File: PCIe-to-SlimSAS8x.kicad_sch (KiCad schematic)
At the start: 11 parts, among them J1 PCI_Express_x8, J2 OpenCAPI_AAC_Host

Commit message: Initial Layout Complete
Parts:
- renumbered R4 to R3, R3 to R4
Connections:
- net GND: now also J2.MP (Shield)
- net PERn0 renamed Rx0_P
- net PERn1 renamed Rx1_P
- net PERn2 renamed Rx2_P
- net PERn3 renamed Rx3_P
- net PERn4 renamed Rx4_P
- net PERn5 renamed Rx5_P
- net PERn6 renamed Rx6_P
- net PERn7 renamed Rx7_P
- net PERp0 renamed Rx0_N
- net PERp1 renamed Rx1_N
- net PERp2 renamed Rx2_N
- net PERp3 renamed Rx3_N
- net PERp4 renamed Rx4_N
- net PERp5 renamed Rx5_N
- net PERp6 renamed Rx6_N
- net PERp7 renamed Rx7_N
- net PETn0 renamed Tx0_N
- net Tx0_N: now also J2.A2 (Tx0_N); no longer J2.A3 (Tx0_P)
- net PETn1 renamed Tx1_N
- net Tx1_N: now also J2.B2 (Tx1_N); no longer J2.B3 (Tx1_P)
- net PETn2 renamed Tx2_N
- net Tx2_N: now also J2.A5 (Tx2_N); no longer J2.A6 (Tx2_P)
- net PETn3 renamed Tx3_N
- net Tx3_N: now also J2.B5 (Tx3_N); no longer J2.B6 (Tx3_P)
- net PETn4 renamed Tx4_N
- net Tx4_N: now also J2.B11 (Tx4_N); no longer J2.B12 (Tx4_P)
- net PETn5 renamed Tx5_N
- net Tx5_N: now also J2.A14 (Tx5_N); no longer J2.A15 (Tx5_P)
- net PETn6 renamed Tx6_N
- net Tx6_N: now also J2.B14 (Tx6_N); no longer J2.B15 (Tx6_P)
- net PETn7 renamed Tx7_N
- net Tx7_N: now also J2.A17 (Tx7_N); no longer J2.A18 (Tx7_P)
- net PETp0 renamed Tx0_P
- net Tx0_P: now also J2.A3 (Tx0_P); no longer J2.A2 (Tx0_N)
- net PETp1 renamed Tx1_P
- net Tx1_P: now also J2.B3 (Tx1_P); no longer J2.B2 (Tx1_N)
- net PETp2 renamed Tx2_P
- net Tx2_P: now also J2.A6 (Tx2_P); no longer J2.A5 (Tx2_N)
- net PETp3 renamed Tx3_P
- net Tx3_P: now also J2.B6 (Tx3_P); no longer J2.B5 (Tx3_N)
- net PETp4 renamed Tx4_P
- net Tx4_P: now also J2.B12 (Tx4_P); no longer J2.B11 (Tx4_N)
- net PETp5 renamed Tx5_P
- net Tx5_P: now also J2.A15 (Tx5_P); no longer J2.A14 (Tx5_N)
- net PETp6 renamed Tx6_P
- net Tx6_P: now also J2.B15 (Tx6_P); no longer J2.B14 (Tx6_N)
- net PETp7 renamed Tx7_P
- net Tx7_P: now also J2.A18 (Tx7_P); no longer J2.A17 (Tx7_N)
- net REFCLKn renamed REFCLK_N
- net REFCLKp renamed REFCLK_P
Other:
- note added: "SlimSAS 8x Cable flips rows of pins. Row A connects to Row B and vice versa. The OpenCAPI AAC FPGA-based Add-In Card uses the Carrier pinout, which means this adapter should use the Host pinout. FPGA_Card_RX = Host_TX = PCIe_TX FPGA_Card_TX = Host_RX = PCIe_RX"
- note removed: "SlimSAS 8i Cable flips rows of pins. Row A connects to Row B and vice versa. The OpenCAPI AAC Add-In Card uses the Carrier pinout, which means this adapter should use the Host pinout. Card_TX = Host_RX = PCIe_RX Card_RX = Host_TX = PCIe_TX"
- title: PCI-Express to OpenCAPI Adapter -> PCI-Express to SlimSAS 8x Adapter
- moved on the sheet: J1, R1, R2, R3, R4, TP1, TP2, TP3, TP4, TP5

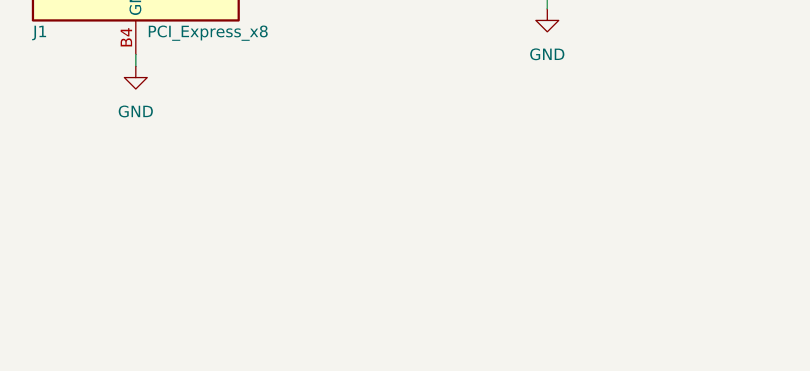
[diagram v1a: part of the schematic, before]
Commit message: Added Microstrip Test Trace
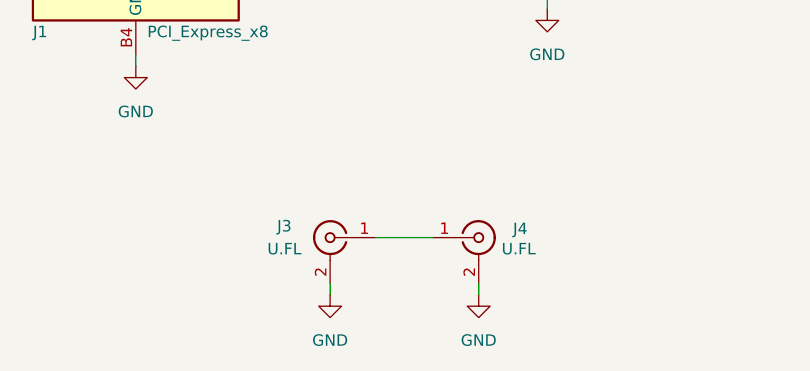
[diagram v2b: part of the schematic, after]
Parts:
- added J3, J4: U.FL, Connector_Coaxial:U.FL_Hirose_U.FL-R-SMT-1_Vertical, symbol Connector:Conn_Coaxial
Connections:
- net GND: now also J3.2 (Ext), J4.2 (Ext)
- new net: J3.1 (In), J4.1 (In)
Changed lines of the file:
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@@
+    (stroke (width 0) (type default) (color 0 0 0 0))
+  )
+  (wire (pts (xy 110.49 175.26) (xy 110.49 176.53))
     (stroke (width 0) (type default) (color 0 0 0 0))
   )
@@
     (stroke (width 0) (type default) (color 0 0 0 0))
   )
+  (wire (pts (xy 127 175.26) (xy 127 176.53))
+    (stroke (width 0) (type default) (color 0 0 0 0))
+  )
   (wire (pts (xy 134.62 142.24) (xy 134.62 144.78))
     (stroke (width 0) (type default) (color 0 0 0 0))
@@
   )
   (wire (pts (xy 171.45 142.24) (xy 176.53 142.24))
+    (stroke (width 0) (type default) (color 0 0 0 0))
+  )
+  (wire (pts (xy 115.57 170.18) (xy 121.92 170.18))
     (stroke (width 0) (type default) (color 0 0 0 0))
   )
@@
     (pin "2")
   )
+  (symbol (lib_id "Connector:Conn_Coaxial") (at 127 170.18 0) (unit 1)
+    (in_bom yes) (on_board yes)
+    (property "Reference" "J4" (id 0) (at 130.81 169.2031 0)
+      (effects (font (size 1.27 1.27)) (justify left))
+    )
+    (property "Value" "U.FL" (id 1) (at 129.54 171.45 0)
+      (effects (font (size 1.27 1.27)) (justify left))
+    )
+    (property "Footprint" "Connector_Coaxial:U.FL_Hirose_U.FL-R-SMT-1_Vertical" (id 2) (at 127 170.18 0)
+      (effects (font (size 1.27 1.27)) hide)
+    )
+    (property "Datasheet" " ~" (id 3) (at 127 170.18 0)
+      (effects (font (size 1.27 1.27)) hide)
+    )
+    (pin "1")
+    (pin "2")
+  )
   (symbol (lib_id "power:GND") (at 88.9 151.13 0) (unit 1)
     (in_bom yes) (on_board yes) (fields_autoplaced)
@@
     (pin "1")
   )
+  (symbol (lib_id "Connector:Conn_Coaxial") (at 110.49 170.18 0) (mirror y) (unit 1)
+    (in_bom yes) (on_board yes)
+    (property "Reference" "J3" (id 0) (at 105.41 168.91 0))
+    (property "Value" "U.FL" (id 1) (at 105.41 171.45 0))
+    (property "Footprint" "Connector_Coaxial:U.FL_Hirose_U.FL-R-SMT-1_Vertical" (id 2) (at 110.49 170.18 0)
+      (effects (font (size 1.27 1.27)) hide)
+    )
+    (property "Datasheet" " ~" (id 3) (at 110.49 170.18 0)
+      (effects (font (size 1.27 1.27)) hide)
+    )
+    (pin "1")
+    (pin "2")
+  )
   (symbol (lib_id "power:GND") (at 134.62 144.78 0) (unit 1)
     (in_bom yes) (on_board yes) (fields_autoplaced)
@@
     (pin "1")
     (pin "2")
+  )
+  (symbol (lib_id "power:GND") (at 127 176.53 0) (unit 1)
+    (in_bom yes) (on_board yes) (fields_autoplaced)
+    (property "Reference" "#PWR0105" (id 0) (at 127 182.88 0)
+      (effects (font (size 1.27 1.27)) hide)
+    )
+    (property "Value" "GND" (id 1) (at 127 181.61 0))
+    (property "Footprint" "" (id 2) (at 127 176.53 0)
+      (effects (font (size 1.27 1.27)) hide)
+    )
+    (property "Datasheet" "" (id 3) (at 127 176.53 0)
+      (effects (font (size 1.27 1.27)) hide)
+    )
+    (pin "1")
   )
   (symbol (lib_id "Connector:Bus_PCI_Express_x8") (at 88.9 104.14 0) (unit 1)
@@
     (pin "B9")
   )
+  (symbol (lib_id "power:GND") (at 110.49 176.53 0) (unit 1)
+    (in_bom yes) (on_board yes) (fields_autoplaced)
+    (property "Reference" "#PWR0106" (id 0) (at 110.49 182.88 0)
+      (effects (font (size 1.27 1.27)) hide)
+    )
+    (property "Value" "GND" (id 1) (at 110.49 181.61 0))
+    (property "Footprint" "" (id 2) (at 110.49 176.53 0)
+      (effects (font (size 1.27 1.27)) hide)
+    )
+    (property "Datasheet" "" (id 3) (at 110.49 176.53 0)
+      (effects (font (size 1.27 1.27)) hide)
+    )
+    (pin "1")
+  )
   (symbol (lib_id "power:GND") (at 209.55 125.73 0) (unit 1)
     (in_bom yes) (on_board yes) (fields_autoplaced)
@@
       (reference "#PWR0104") (unit 1) (value "GND") (footprint "")
     )
+    (path "/985c76e3-f752-431f-8993-ae16c4190f4d"
+      (reference "#PWR0105") (unit 1) (value "GND") (footprint "")
+    )
+    (path "/ae0a2e17-be81-471b-ad82-f20fc8a6739c"
+      (reference "#PWR0106") (unit 1) (value "GND") (footprint "")
+    )
     (path "/add1d7a7-6758-4be8-986d-7ced6599002b"
       (reference "J1") (unit 1) (value "PCI_Express_x8") (footprint "Connector_PCBEdge:BUS_PCIexpress_x8")
@@
       (reference "J2") (unit 1) (value "OpenCAPI_AAC_Host") (footprint "SlimSAS_8x:SlimSAS_8x_RA_U10-A474")
     )
+    (path "/1471c926-c8ce-42b7-9d66-a42cdcd84ad4"
+      (reference "J3") (unit 1) (value "U.FL") (footprint "Connector_Coaxial:U.FL_Hirose_U.FL-R-SMT-1_Vertical")
+    )
+    (path "/033ef903-ec47-4362-a6c2-b01118e4fe96"
+      (reference "J4") (unit 1) (value "U.FL") (footprint "Connector_Coaxial:U.FL_Hirose_U.FL-R-SMT-1_Vertical")
+    )
     (path "/00ff3368-9ed6-4bd3-a145-54019cd019df"

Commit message: Rev2 Schematic
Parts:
- removed TP1: SCL, Connector_PinHeader_2.54mm:PinHeader_1x01_P2.54mm_Vertical, symbol Connector:TestPoint
- removed TP2: SDA, Connector_PinHeader_2.54mm:PinHeader_1x01_P2.54mm_Vertical, symbol Connector:TestPoint
- removed TP3: PRE, Connector_PinHeader_2.54mm:PinHeader_1x01_P2.54mm_Vertical, symbol Connector:TestPoint
- removed TP4: 3V3, Connector_PinHeader_2.54mm:PinHeader_1x01_P2.54mm_Vertical, symbol Connector:TestPoint
- removed TP5: GND, Connector_PinHeader_2.54mm:PinHeader_1x01_P2.54mm_Vertical, symbol Connector:TestPoint
- added J5, J6: U.FL, Connector_Coaxial:U.FL_Hirose_U.FL-R-SMT-1_Vertical, symbol Connector:Conn_Coaxial
- added J7: EXTRA, Connector_PinHeader_2.54mm:PinHeader_1x06_P2.54mm_Vertical, symbol Connector_Generic:Conn_01x06
- added R5: DNP, Resistor_SMD:R_0603_1608Metric, symbol Device:R_Small
- added TP6: PRSNT1, Connector_PinHeader_1.00mm:PinHeader_1x01_P1.00mm_Vertical, symbol Connector:TestPoint
- added TP7: PRSNT2_x1, Connector_PinHeader_1.00mm:PinHeader_1x01_P1.00mm_Vertical, symbol Connector:TestPoint
- added TP8: PRSNT2_x4, Connector_PinHeader_1.00mm:PinHeader_1x01_P1.00mm_Vertical, symbol Connector:TestPoint
- added TP9: PRSNT2_x8, Connector_PinHeader_1.00mm:PinHeader_1x01_P1.00mm_Vertical, symbol Connector:TestPoint
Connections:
- net GND: now also J5.2 (Ext), J6.2 (Ext), J7.6 (Pin_6)
- net Rx0_N: now also J1.A17 (PERn0), J2.A3 (Rx0_N); no longer J1.A16 (PERp0), J2.A23 (Rx0_N)
- net Rx0_P: now also J1.A16 (PERp0), J2.A2 (Rx0_P); no longer J1.A17 (PERn0), J2.A24 (Rx0_P)
- net Rx1_N: now also J1.A22 (PERn1), J2.B3 (Rx1_N); no longer J1.A21 (PERp1), J2.B20 (Rx1_N)
- net Rx1_P: now also J1.A21 (PERp1), J2.B2 (Rx1_P); no longer J1.A22 (PERn1), J2.B21 (Rx1_P)
- net Rx2_N: now also J1.A26 (PERn2), J2.A6 (Rx2_N); no longer J1.A25 (PERp2), J2.A26 (Rx2_N)
- net Rx2_P: now also J1.A25 (PERp2), J2.A5 (Rx2_P); no longer J1.A26 (PERn2), J2.A27 (Rx2_P)
- net Rx3_N: now also J1.A30 (PERn3), J2.B6 (Rx3_N); no longer J1.A29 (PERp3), J2.B23 (Rx3_N)
- net Rx3_P: now also J1.A29 (PERp3), J2.B5 (Rx3_P); no longer J1.A30 (PERn3), J2.B24 (Rx3_P)
- net Rx4_N: now also J1.A36 (PERn4), J2.B12 (Rx4_N); no longer J1.A35 (PERp4), J2.B29 (Rx4_N)
- net Rx4_P: now also J1.A35 (PERp4), J2.B11 (Rx4_P); no longer J1.A36 (PERn4), J2.B30 (Rx4_P)
- net Rx5_N: now also J1.A40 (PERn5), J2.A15 (Rx5_N); no longer J1.A39 (PERp5), J2.A35 (Rx5_N)
- net Rx5_P: now also J1.A39 (PERp5), J2.A14 (Rx5_P); no longer J1.A40 (PERn5), J2.A36 (Rx5_P)
- net Rx6_N: now also J1.A44 (PERn6), J2.B15 (Rx6_N); no longer J1.A43 (PERp6), J2.B32 (Rx6_N)
- net Rx6_P: now also J1.A43 (PERp6), J2.B14 (Rx6_P); no longer J1.A44 (PERn6), J2.B33 (Rx6_P)
- net Rx7_N: now also J1.A48 (PERn7), J2.A18 (Rx7_N); no longer J1.A47 (PERp7), J2.B35 (Rx7_N)
- net Rx7_P: now also J1.A47 (PERp7), J2.A17 (Rx7_P); no longer J1.A48 (PERn7), J2.B36 (Rx7_P)
- net SCL: now also J7.2 (Pin_2)
- net SDA: now also J7.3 (Pin_3)
- net Tx0_N: now also J2.B36 (Tx0_N); no longer J2.A2 (Tx0_N)
- net Tx0_P: now also J2.B35 (Tx0_P); no longer J2.A3 (Tx0_P)
- net Tx1_N: now also J2.B33 (Tx1_N); no longer J2.B2 (Tx1_N)
- net Tx1_P: now also J2.B32 (Tx1_P); no longer J2.B3 (Tx1_P)
- net Tx2_N: now also J2.A36 (Tx2_N); no longer J2.A5 (Tx2_N)
- net Tx2_P: now also J2.A35 (Tx2_P); no longer J2.A6 (Tx2_P)
- net Tx3_N: now also J2.B30 (Tx3_N); no longer J2.B5 (Tx3_N)
- net Tx3_P: now also J2.B29 (Tx3_P); no longer J2.B6 (Tx3_P)
- net Tx4_N: now also J2.B24 (Tx4_N); no longer J2.B11 (Tx4_N)
- net Tx4_P: now also J2.B23 (Tx4_P); no longer J2.B12 (Tx4_P)
- net Tx5_N: now also J2.A27 (Tx5_N); no longer J2.A14 (Tx5_N)
- net Tx5_P: now also J2.A26 (Tx5_P); no longer J2.A15 (Tx5_P)
- net Tx6_N: now also J2.B21 (Tx6_N); no longer J2.B14 (Tx6_N)
- net Tx6_P: now also J2.B20 (Tx6_P); no longer J2.B15 (Tx6_P)
- net Tx7_N: now also J2.A24 (Tx7_N); no longer J2.A17 (Tx7_N)
- net Tx7_P: now also J2.A23 (Tx7_P); no longer J2.A18 (Tx7_P)
- net nPERST: now also J7.1 (Pin_1)
- net TST_P: now reaches J3.1 (In), J4.1 (In)
- net at J1.A1 (~{PRSNT1}): now also J1.B48 (~{PRSNT2}), R5.1, R5.2, TP6.1, TP9.1
- net at J1.B17 (~{PRSNT2}): now also TP7.1
- net at J1.B31 (~{PRSNT2}): now also TP8.1
- net 3V3 renamed +3.3V
- net +3.3V: now also J7.5 (Pin_5)
- net PRE renamed PRE_DETECT
- net PRE_DETECT: now also J7.4 (Pin_4)
- new net TST_N: J5.1 (In), J6.1 (In)
- no-connect marks 29 -> 25
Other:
- note added: "I2C SCL and SDA operate at 3.3V"
- moved on the sheet: J1
